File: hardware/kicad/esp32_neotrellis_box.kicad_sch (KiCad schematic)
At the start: 25 parts, among them J1 USB_C_Receptacle, J2 12V_IN, J3 NeoTrellis_JST_PH, Q1 AO3401A, U1 ESP32-C3-Super-Mini, U2 TP4056, U3 AMS1117-3.3, U4 MP1584EN

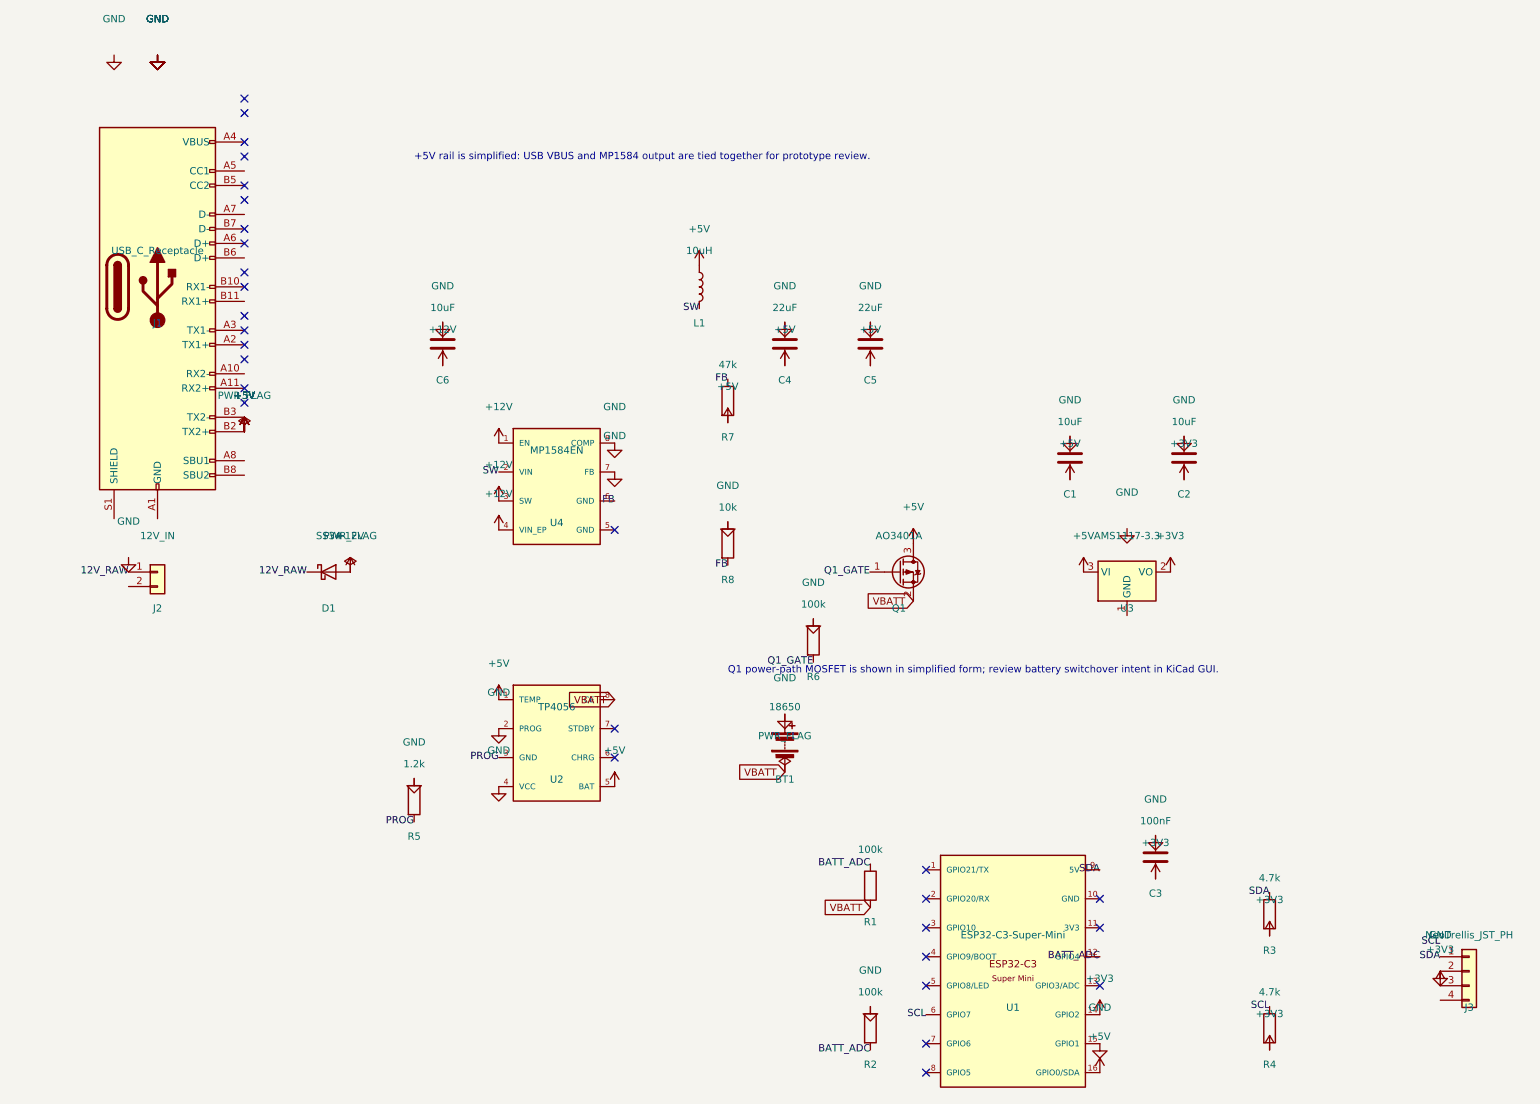
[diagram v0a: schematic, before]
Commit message: Phase 2: rewrite KiCAD schematic with label-based connectivity
Fix broken net connections from v1. All components now connected
via net labels/power symbols placed directly at pin endpoints.
Validated by kicad-cli sch export netlist.

Co-authored-by: Copilot <223556219+Copilot@users.noreply.github.com>
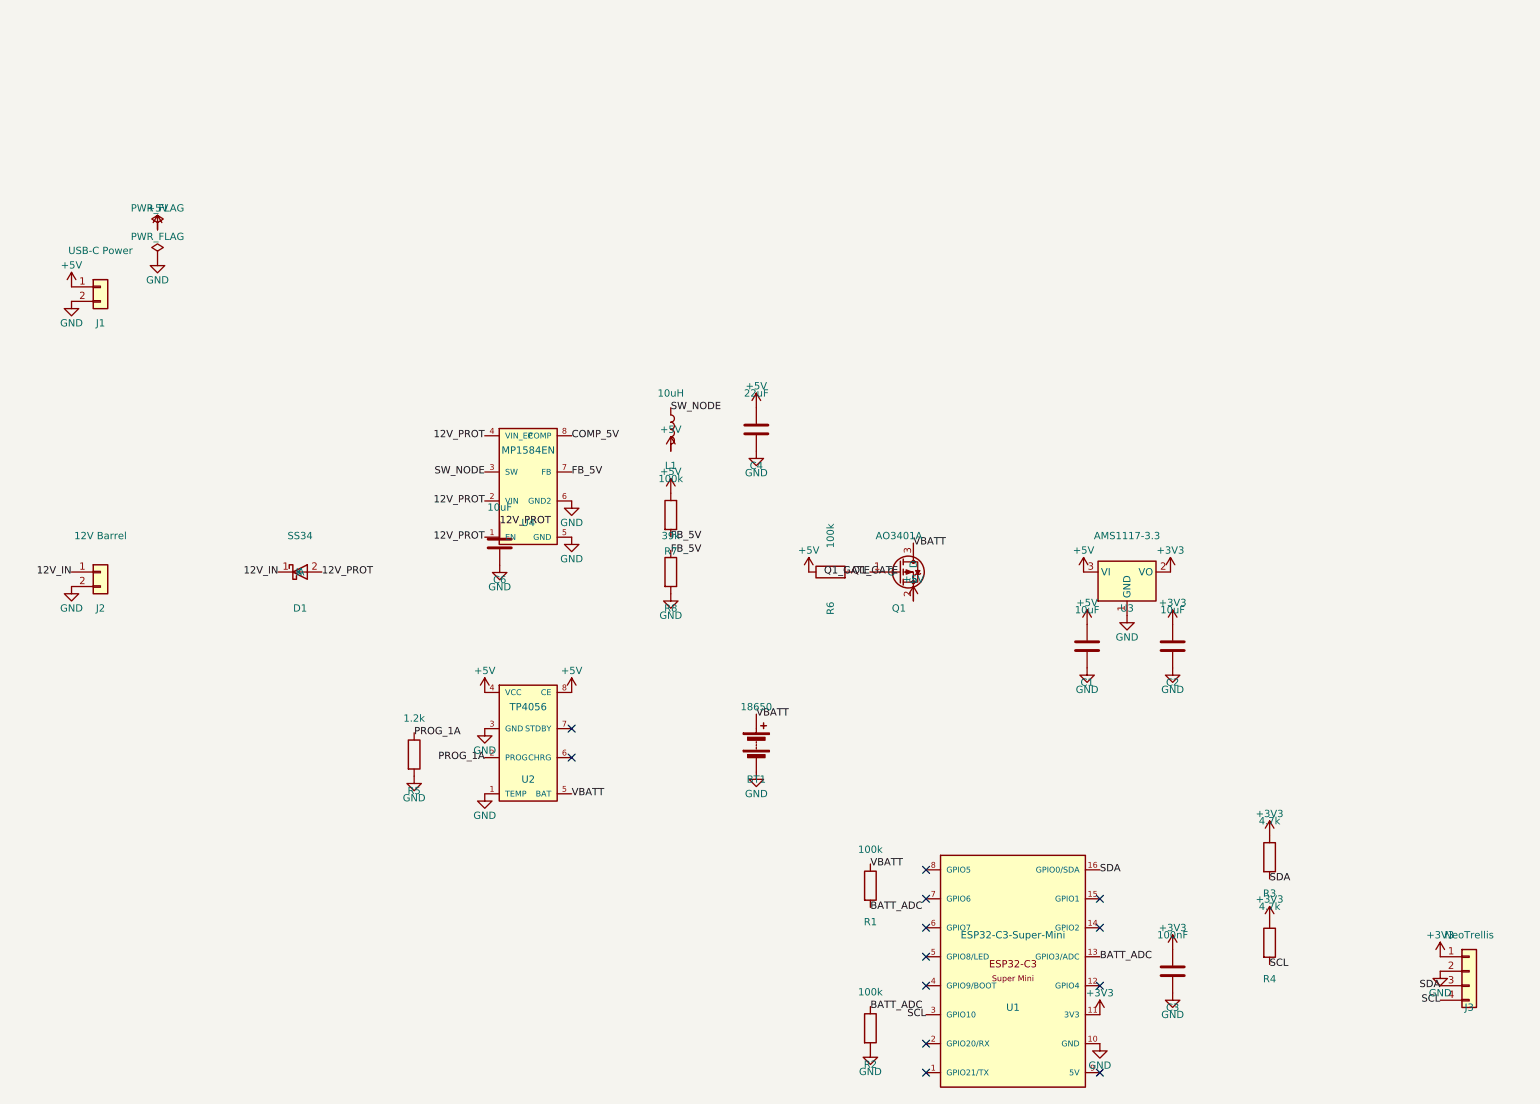
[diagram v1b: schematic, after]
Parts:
- removed C5: 22uF, symbol Device:C
- removed J1: USB_C_Receptacle, symbol Connector:USB_C_Receptacle
- added J1: USB-C Power, symbol Connector_Generic:Conn_01x02
- J2: value 12V_IN -> 12V Barrel
- J3: value NeoTrellis_JST_PH -> NeoTrellis
- R7: value 47k -> 100k
- R8: value 10k -> 39k
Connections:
- net PROG is gone; now on net GND: R5.2, U2.3 (GND)
- net +3V3: now also C2.1, C3.1, J3.1 (Pin_1), R3.1, R4.1, U1.11 (3V3); no longer C2.2, C3.2, J3.3 (Pin_3), R3.2, R4.2, U1.14 (GPIO2)
- net +5V: now also C1.1, C4.1, L1.2, Q1.2 (S), R6.1, R7.1, U2.4 (VCC), U2.8 (CE), J1.1 (Pin_1); no longer C1.2, C4.2, L1.1, Q1.3 (D), R7.2, U1.16 (GPIO0/SDA), U2.1 (TEMP), U2.5 (BAT)
- net BATT_ADC: now also R1.2, R2.1, U1.13 (GPIO3/ADC); no longer R1.1, R2.2, U1.12 (GPIO4)
- net GND: now also BT1.2 (-), C1.2, C2.2, C3.2, C4.2, C6.2, J2.2 (Pin_2), R2.2, R8.2, U1.10 (GND), U2.1 (TEMP), U3.1 (GND), U4.5 (GND), U4.6 (GND2), J1.2 (Pin_2); no longer BT1.1 (+), C1.1, C2.1, C3.1, C4.1, C6.1, R2.1, R5.1, R6.1, R8.1, U1.15 (GPIO1), U2.2 (PROG), U2.4 (VCC), U4.7 (FB), U4.8 (COMP)
- net SCL: now also J3.4 (Pin_4), R4.2, U1.3 (GPIO10); no longer R4.1, U1.6 (GPIO7)
- net SDA: now also J3.3 (Pin_3), R3.2, U1.16 (GPIO0/SDA); no longer J3.1 (Pin_1), R3.1, U1.9 (5V)
- net VBATT: now also BT1.1 (+), Q1.3 (D), R1.1, U2.5 (BAT); no longer BT1.2 (-), Q1.2 (S), R1.2, U2.8 (CE)
- net +12V renamed 12V_PROT
- net 12V_PROT: now also C6.1, U4.2 (VIN); no longer C6.2, U4.3 (SW)
- net 12V_RAW renamed 12V_IN
- removed net FB: R7.1, R8.2, U4.6 (GND)
- removed net SW: L1.2, U4.2 (VIN)
- new net COMP_5V: U4.8 (COMP)
- new net FB_5V: R7.2, R8.1, U4.7 (FB)
- new net PROG_1A: R5.1, U2.2 (PROG)
- new net SW_NODE: L1.1, U4.3 (SW)
- no-connect marks 29 -> 13
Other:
- note removed: "+5V rail is simplified: USB VBUS and MP1584 output are tied together for prototype review."
- note removed: "Q1 power-path MOSFET is shown in simplified form; review battery switchover intent in KiCad GUI."

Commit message: Phase 2 complete: KiCAD schematic with correct net connectivity
Fix critical bug in schematic generator: KiCAD symbol coordinates
use Y-up convention (symbol editor), but schematic uses Y-down.
Correct formula: sch_y = cy - sym_y (Y is negated on placement).

Empirically verified pin positions for all component types:
  Device:R/C/L: pin1 at (cx, cy-3.81), pin2 at (cx, cy+3.81)
  Device:Battery: pin+(1) at (cy-5.08), pin-(2) at (cy+5.08)
  Conn_01x02: pin1 at (cx-5.08, cy), pin2 at (cx-5.08, cy+2.54)
  Conn_01x04: pin1..4 at cy-2.54, cy, cy+2.54, cy+5.08
  AMS1117-3.3: GND at cy+7.62, VO at cx+7.62, VI at cx-7.62
  AO3401A: G at cx-5.08, S at cy+5.08, D at cy-5.08

Also fixed lib_sym() symbol extraction bugs:
  - Resolved catastrophic regex backtracking (hang)
  - Properly resolves extends by inlining parent geometry
  - Added pin UUID entries to component instances

Validated netlist: all 7 key nets correct
  +3V3: U1[11], U3[2], J3[1], R3[1], R4[1], C2[1], C3[1]
  +5V: J1[1], L1[2], Q1[2], U3[3], U2[4], U2[8], C1[1]
  GND: U1[10], U2[1], U2[3], U3[1], BT1[2], J1[2]...(18)
  VBATT: BT1[1], Q1[3], R1[1], U2[5]
  SDA: U1[16], J3[3], R3[2]
  SCL: U1[3], J3[4], R4[2]
  BATT_ADC: U1[13], R1[2], R2[1]

13 intentional unconnected pins (unused GPIOs, LED pins).

Co-authored-by: Copilot <223556219+Copilot@users.noreply.github.com>
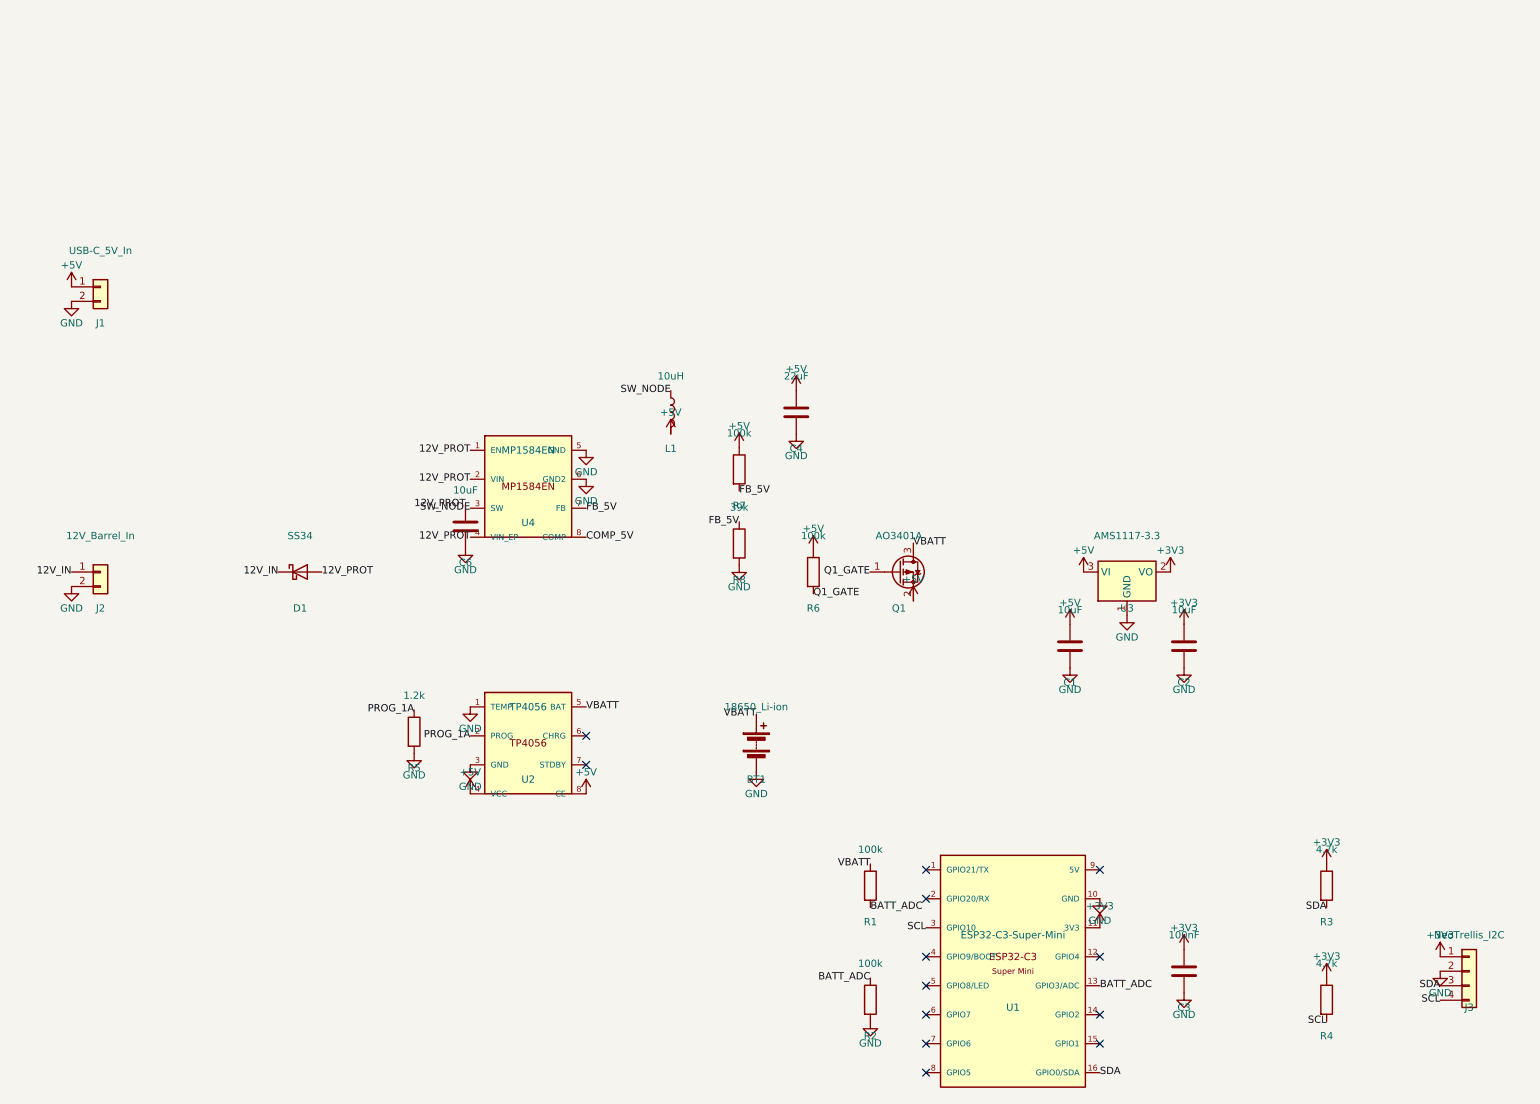
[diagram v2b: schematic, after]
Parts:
- BT1: value 18650 -> 18650_Li-ion
- D1: footprint Diode_SMD:D_SMA -> (none)
- J1: value USB-C Power -> USB-C_5V_In
- J2: value 12V Barrel -> 12V_Barrel_In
- J3: value NeoTrellis -> NeoTrellis_I2C
- Q1: footprint Package_TO_SOT_SMD:SOT-23 -> (none)
- U2, U4: footprint Package_SO:SOP-8_3.9x4.9mm_P1.27mm -> (none)
- U3: footprint Package_TO_SOT_SMD:SOT-223-3_TabPin2 -> (none)

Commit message: Add wire stubs to schematic for visual connectivity
Every pin connection now has a 2.54mm wire stub extending
from the pin endpoint outward from the component body,
with the net label or power symbol at the stub end.

This makes the schematic visually readable in KiCAD:
- Labels/power symbols appear as flags on short wires
- Components no longer look isolated
- All 7 key nets validated correct (unchanged)

65 wire stubs added.

Co-authored-by: Copilot <223556219+Copilot@users.noreply.github.com>
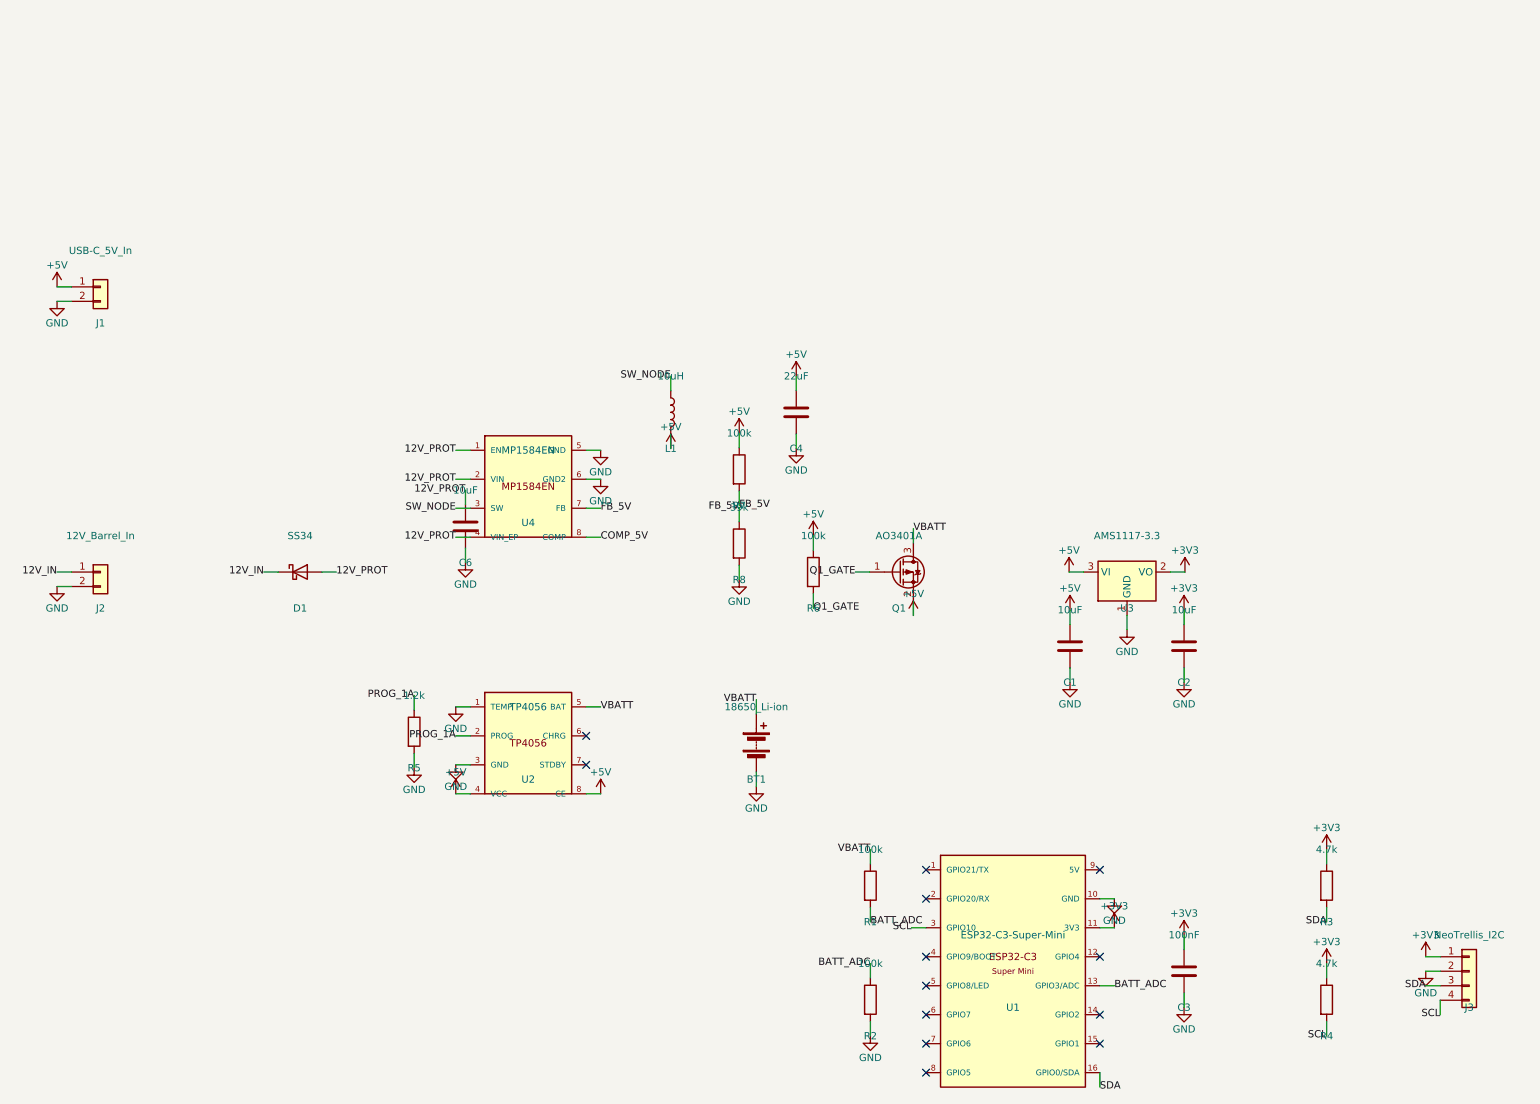
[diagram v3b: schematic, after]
